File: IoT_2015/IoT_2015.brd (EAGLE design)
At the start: 100 x 80 mm, 29 parts, among them Y1 ABLS-16.000MHZ-B4-T

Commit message: First board design finished
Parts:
- removed HUM/TEMP: SHTC1, Sensirion:4INPUTS
- added SI7006: SI7006-A20-IM, SiliconLabs:SI7006-A20-IM
- moved R4 73.1 mm to (33.0, 6.35)
- moved C11 67.9 mm to (17.8, 8.89)
- moved R3 67.1 mm to (33.0, 8.89)
- moved C12 66.6 mm to (17.8, 6.35)
- moved C6 65.2 mm to (14.0, 11.4)
- moved JTAG 64.4 mm to (33.0, 2.54)
- moved C7 64.0 mm to (14.0, 8.89)
- moved C8 62.7 mm to (14.0, 6.35)
- moved C1 62.6 mm to (10.2, 14.0)
- moved C2 61.3 mm to (10.2, 11.4)
- moved R2 61.1 mm to (33.0, 11.4)
- moved L5 61.0 mm to (6.35, 16.5)
- moved C3 60.0 mm to (10.2, 8.89)
- moved L4 59.7 mm to (6.35, 14.0)
- moved C4 58.8 mm to (10.2, 6.35)
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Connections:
- net GND: now also SI7006.GND; no longer HUM/TEMP.VSS
- net SCL: now also SI7006.SCL; no longer HUM/TEMP.SCL
- net SDA: now also SI7006.SDA; no longer HUM/TEMP.SDA
- net VDD: now also SI7006.VDD; no longer HUM/TEMP.VDD
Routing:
- net VDD: track 0.00 -> 80.9 mm, vias 0 -> 1
- net GND: track 0.00 -> 67.3 mm, vias 0 -> 1
- net N$4: track 0.00 -> 41.5 mm, vias 0 -> 3
- net N$11: track 0.00 -> 23.4 mm, vias 0 -> 2
- net N$5: track 0.00 -> 16.1 mm, vias 0 -> 2
- net N$10: track 0.00 -> 15.3 mm, vias 0 -> 2
- net N$7: track 0.00 -> 14.1 mm, vias 0 -> 2
- net N$9: track 0.00 -> 11.5 mm
- net SCL: track 0.00 -> 11.2 mm, vias 0 -> 2
- net SWDCLK: track 0.00 -> 10.5 mm
- net SDA: track 0.00 -> 4.32 mm
- net N$6: track 0.00 -> 3.59 mm
- net N$1: track 0.00 -> 3.43 mm
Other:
- board size 100 x 80 mm -> 40 x 20 mm
- board text added: "BlueNinc"

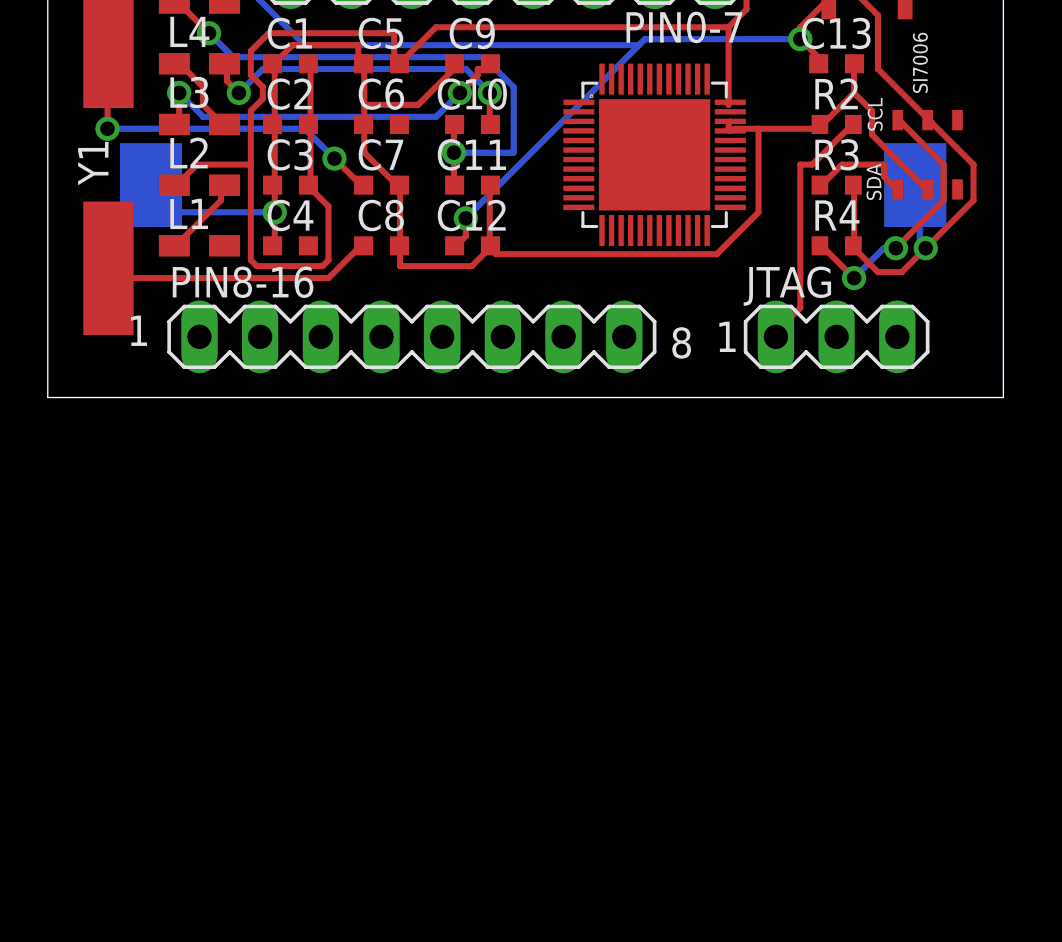
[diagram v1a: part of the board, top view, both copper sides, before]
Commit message: Refining
Changed the battery holder, deleted some pinheaders
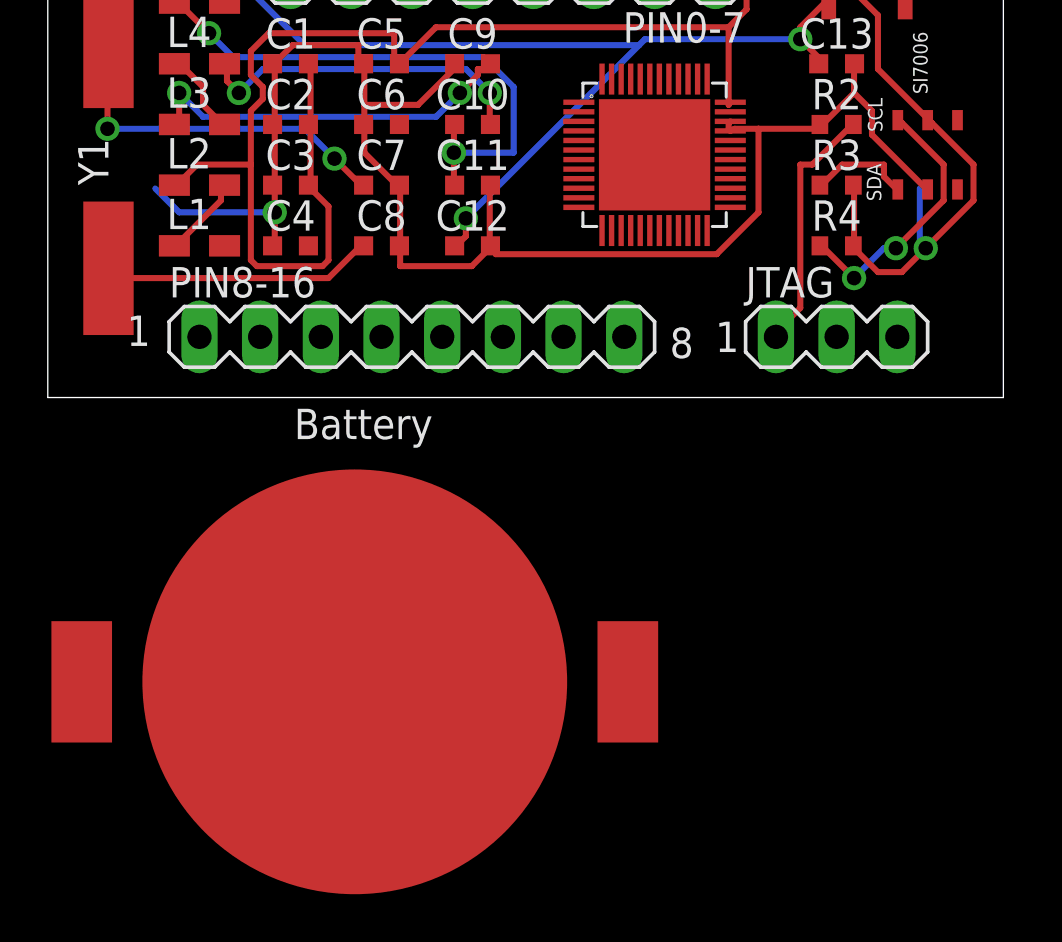
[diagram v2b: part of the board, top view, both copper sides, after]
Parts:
- removed BATTERY: SMTU2032-G.TR, Renata:SMTU2032-G.TR
- added U$2: BAT-HLD-001, BAT-HLD-001:BAT-HLD-001
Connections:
- net GND: now also U$2.GND; no longer BATTERY.GND
- net VDD: now also U$2.VDD1, U$2.VDD2; no longer BATTERY.VCC
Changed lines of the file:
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@@
 <?xml version="1.0" encoding="utf-8"?>
 <!DOCTYPE eagle SYSTEM "eagle.dtd">
-<eagle version="7.3.0">
+<eagle version="7.2.0">
 <drawing>
 <settings>
@@
 <elements>
 <element name="ANTENNA" library="Pulse" package="W3008" value="W3008" x="34.29" y="16.51"/>
-<element name="BATTERY" library="Renata" package="SMTU2032-G.TR" value="SMTU2032-G.TR" x="20.32" y="8.89" rot="MR0"/>
 <element name="C1" library="Vishay" package="VJ1603_W1BC" value="" x="10.16" y="13.97"/>
 <element name="C10" library="Vishay" package="VJ1603_W1BC" value="" x="17.78" y="11.43"/>
@@
 <element name="Y1" library="Abracon" package="ABLS-16.000MHZ-B4-T" value="ABLS-16.000MHZ-B4-T" x="2.54" y="10.16" rot="R90"/>
 <element name="SI7006" library="SiliconLabs" package="SI7006-A20-IM" value="SI7006-A20-IM" x="36.83" y="10.16" rot="R90"/>
+<element name="U$2" library="BAT-HLD-001" package="BAT-HLD-001" value="BAT-HLD-001" x="12.85" y="-11.9"/>
 </elements>
 <signals>
@@
 <contactref element="U$1" pad="35"/>
 <contactref element="C5" pad="E2"/>
-<contactref element="BATTERY" pad="VCC"/>
 <contactref element="R3" pad="E2"/>
 <contactref element="R4" pad="E2"/>
@@
 <wire x1="36.5" y1="6.25" x2="36.5" y2="8.75" width="0.254" layer="16"/>
 <wire x1="36.75" y1="6.25" x2="36.5" y2="6.25" width="0.254" layer="16"/>
-<wire x1="36.5" y1="8.75" x2="36.32" y2="8.89" width="0.254" layer="16"/>
 <wire x1="16.25" y1="15.5" x2="14.72" y2="13.97" width="0.254" layer="1"/>
 <wire x1="28.5" y1="15.5" x2="16.25" y2="15.5" width="0.254" layer="1"/>
@@
 <wire x1="14.5" y1="14" x2="14.72" y2="13.97" width="0.254" layer="1"/>
 <via x="36.75" y="6.25" extent="1-16" drill="0.6096"/>
+<contactref element="U$2" pad="VDD1"/>
+<contactref element="U$2" pad="VDD2"/>
 <wire x1="28.5" y1="12.25" x2="28.57" y2="11.96" width="0" layer="19" extent="1-1"/>
 <wire x1="22.23" y1="12.36" x2="28.5" y2="12.25" width="0" layer="19" extent="1-1"/>
 <wire x1="22.23" y1="7.96" x2="22.23" y2="12.36" width="0" layer="19" extent="1-1"/>
+<wire x1="1.42" y1="-11.9" x2="8.75" y2="5.5" width="0" layer="19" extent="1-1"/>
+<wire x1="24.28" y1="-11.9" x2="22.23" y2="7.96" width="0" layer="19" extent="1-1"/>
 </signal>
 <signal name="N$1">
@@
 <contactref element="C12" pad="E2"/>
 <contactref element="C11" pad="E2"/>
-<contactref element="BATTERY" pad="GND"/>
 <contactref element="R2" pad="E1"/>
 <contactref element="C13" pad="E2"/>
@@
 <wire x1="5.5" y1="7.75" x2="4.5" y2="8.75" width="0.254" layer="16"/>
 <wire x1="9.5" y1="7.75" x2="5.5" y2="7.75" width="0.254" layer="16"/>
-<wire x1="4.5" y1="8.75" x2="4.32" y2="8.89" width="0.254" layer="16"/>
 <wire x1="29.75" y1="7.75" x2="29.75" y2="11.25" width="0.254" layer="1"/>
 <wire x1="28" y1="6" x2="29.75" y2="7.75" width="0.254" layer="1"/>
@@
 <wire x1="18.75" y1="6.25" x2="18.53" y2="6.35" width="0.254" layer="1"/>
 <via x="9.5" y="7.75" extent="1-16" drill="0.6096"/>
+<contactref element="U$2" pad="GND"/>
 <wire x1="18.75" y1="6.25" x2="23.2" y2="6.99" width="0" layer="19" extent="1-1"/>
+<wire x1="12.85" y1="-11.9" x2="14.75" y2="5.5" width="0" layer="19" extent="1-1"/>
 </signal>
 <signal name="N$3">

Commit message: Finished design
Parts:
- removed PIN0-7, PIN8-16: (no value), con-lstb:MA08-1
- removed U$2: BAT-HLD-001, BAT-HLD-001:BAT-HLD-001
- added BATTERY: BAT-HLD-001, BAT-HLD-001:BAT-HLD-001
- added P02, P35, P67VDD: (no value), con-lstb:MA03-1
- moved JTAG 32.5 mm to (4.38, 17.9), turned to 180 degrees
- moved SI7006 30.8 mm to (6.19, 6.61), turned to 0 degrees
- moved R4 28.6 mm to (4.65, 9.87)
- moved R2 28.3 mm to (4.71, 12.7)
- moved R3 25.4 mm to (7.61, 9.87)
- moved C10 16.9 mm to (1.86, 5.76)
- moved L2 16.8 mm to (20.7, 17.7), turned to 90 degrees
- moved C12 16.7 mm to (1.75, 11.1)
- moved C11 16.0 mm to (1.78, 8.46)
- moved Y1 14.4 mm to (16.3, 14.2), turned to 0 degrees
- moved C2 13.9 mm to (24.1, 10.6)
- moved C5 13.4 mm to (24.1, 5.32)
- moved L3 13.0 mm to (17.8, 17.6), turned to 90 degrees
- moved C1 11.4 mm to (21.0, 10.6)
- moved U$1 11.3 mm to (15.1, 5.55)
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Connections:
- removed net P0.08: PIN8-16.1, U$1.14
- removed net P0.09: PIN8-16.2, U$1.15
- removed net P0.10: PIN8-16.3, U$1.16
- removed net P0.11: PIN8-16.4, U$1.17
- removed net P0.12: PIN8-16.5, U$1.18
- removed net P0.13: PIN8-16.6, U$1.19
- removed net P0.14: PIN8-16.7, U$1.20
- removed net P0.15: PIN8-16.8, U$1.21
- net GND: now also BATTERY.GND, JTAG.3; no longer U$2.GND
- net P0.00: now also P02.1; no longer PIN0-7.1
- net P0.01: now also P02.2; no longer PIN0-7.2
- net P0.02: now also P02.3; no longer PIN0-7.3
- net P0.03: now also P35.1; no longer PIN0-7.4
- net P0.04: now also P35.2; no longer PIN0-7.5
- net P0.05: now also P35.3; no longer PIN0-7.6
- net P0.06: now also P67VDD.1; no longer PIN0-7.7
- net P0.07: now also P67VDD.2; no longer PIN0-7.8
- net VDD: now also BATTERY.VDD1, BATTERY.VDD2, P67VDD.3; no longer U$2.VDD1, U$2.VDD2
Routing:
- net N$4: track 41.5 -> 2.71 mm, vias 3 -> 0
- net GND: track 67.1 -> 101.1 mm
- net N$11: track 23.4 -> 0.00 mm, vias 2 -> 0
- net N$7: track 14.1 -> 0.00 mm, vias 2 -> 0
- net SWDCLK: track 10.5 -> 0.00 mm
- net N$5: track 16.1 -> 5.96 mm, vias 2 -> 0
- net N$10: track 15.3 -> 7.14 mm, vias 2 -> 0
- net SCL: track 11.2 -> 6.56 mm, vias 2 -> 0
- net VDD: track 80.7 -> 84.6 mm
- net N$1: track 3.43 -> 0.00 mm
- net SDA: track 4.32 -> 3.04 mm
- net N$9: track 11.5 -> 11.9 mm, vias 0 -> 2
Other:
- board size 40 x 20 mm -> 30 x 20 mm
- board text added: "1"
- board text added: "GND"
- board text added: "JTAG"
- board text added: "P0-2"
- board text added: "P3-5"
- board text added: "P6-7"
- board text added: "VDD"
- board text removed: "BlueNinc"

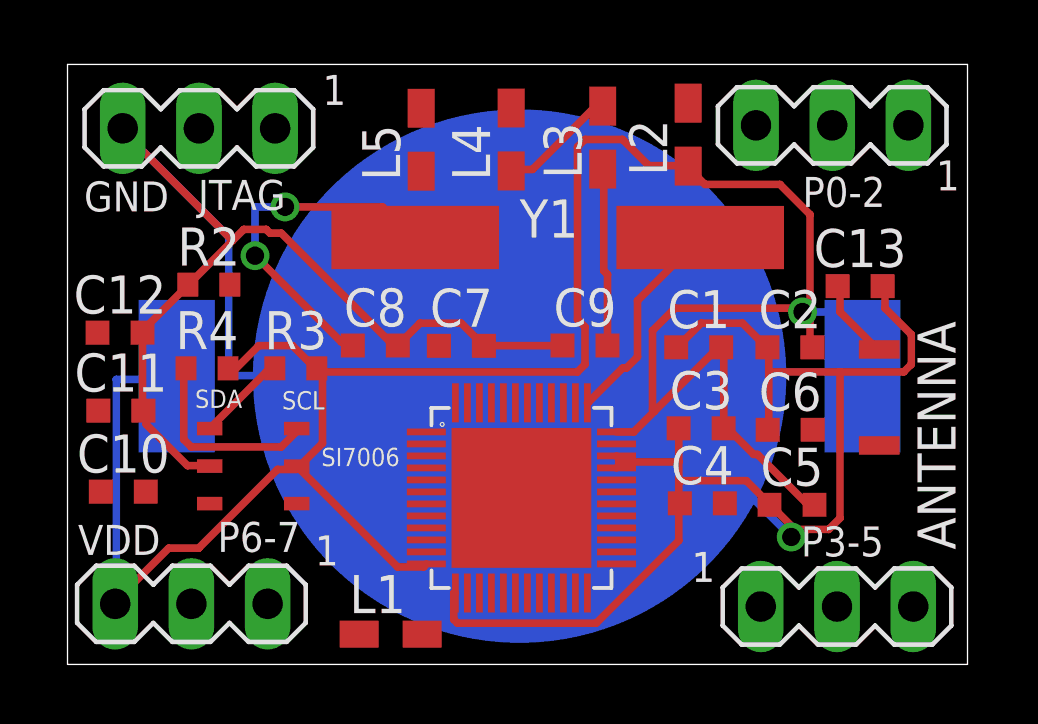
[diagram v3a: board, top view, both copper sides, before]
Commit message: Routed by hand
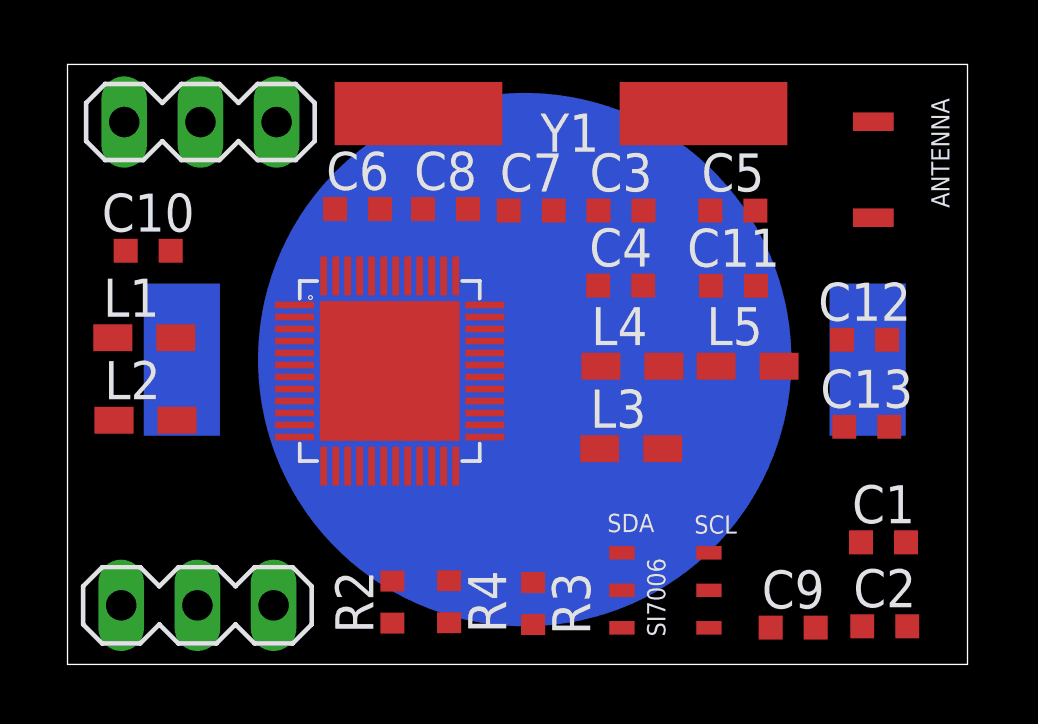
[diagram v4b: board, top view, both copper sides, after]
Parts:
- removed P02, P35: (no value), con-lstb:MA03-1
- moved C12 24.8 mm to (26.6, 10.8)
- moved C11 20.8 mm to (22.2, 12.6)
- moved L2 20.4 mm to (2.60, 8.14), turned to 0 degrees
- moved C6 16.2 mm to (9.67, 15.2)
- moved P67VDD 16.1 mm to (4.43, 18.1), turned to 0 degrees
- moved JTAG 15.9 mm to (4.33, 1.97), turned to 0 degrees
- moved SI7006 14.4 mm to (19.9, 2.47)
- moved L5 13.2 mm to (22.7, 9.94), turned to 0 degrees
- moved L1 12.8 mm to (2.56, 10.9)
- moved R2 12.2 mm to (10.8, 2.08), turned to 90 degrees
- moved C9 11.7 mm to (24.2, 1.23)
- moved R4 11.2 mm to (12.7, 2.09), turned to 270 degrees
- moved R3 11.1 mm to (15.5, 2.03), turned to 270 degrees
- moved L3 10.4 mm to (18.8, 7.19), turned to 0 degrees
- moved C5 10.0 mm to (22.2, 15.1)
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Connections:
- net P0.00: no longer P02.1
- net P0.01: no longer P02.2
- net P0.02: no longer P02.3
- net P0.03: no longer P35.1
- net P0.04: no longer P35.2
- net P0.05: no longer P35.3
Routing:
- net GND: track 101.1 -> 0.00 mm, vias 1 -> 0
- net VDD: track 84.6 -> 0.00 mm, vias 1 -> 0
- net N$9: track 11.9 -> 0.00 mm, vias 2 -> 0
- net SCL: track 6.56 -> 0.00 mm
- net N$5: track 5.96 -> 0.00 mm
- net N$10: track 7.14 -> 3.16 mm
- net N$6: track 3.94 -> 0.00 mm
- net SDA: track 3.04 -> 0.00 mm
- net N$4: track 2.71 -> 0.00 mm
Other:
- board text removed: "1"
- board text removed: "GND"
- board text removed: "JTAG"
- board text removed: "P0-2"
- board text removed: "P3-5"
- board text removed: "P6-7"
- board text removed: "VDD"
